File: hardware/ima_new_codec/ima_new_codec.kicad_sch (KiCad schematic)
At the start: 5 parts, among them J1 DM3AT-SF-PEJM5, U1 STM32F722RETx, Y3 Crystal_GND24

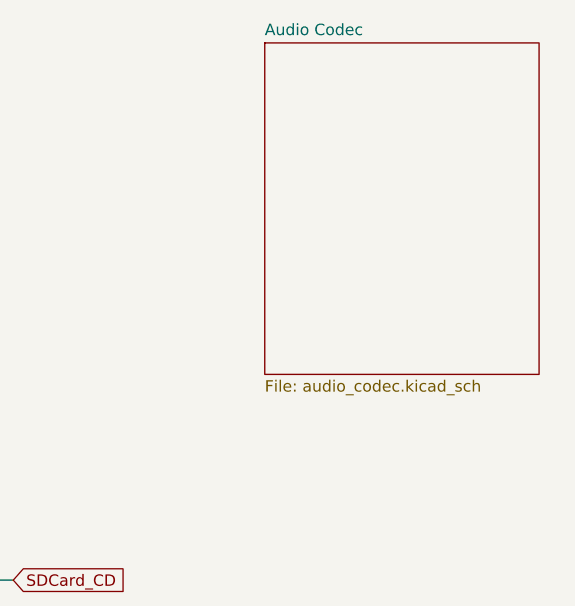
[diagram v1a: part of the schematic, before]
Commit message: changes to in/out stages
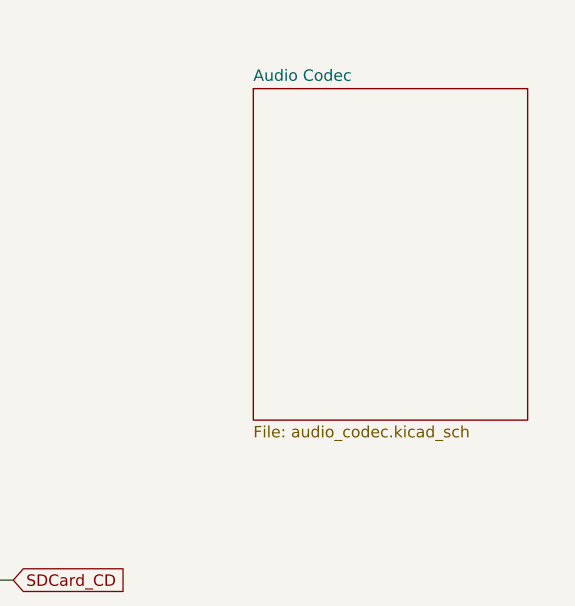
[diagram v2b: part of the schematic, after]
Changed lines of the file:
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@@
 	)
 	(sheet
-		(at 212.09 30.48)
+		(at 210.82 35.56)
 		(size 30.48 36.83)
 		(fields_autoplaced yes)
@@
 		)
 		(property "Sheetname" "Audio Codec"
-			(at 212.09 29.7684 0)
+			(at 210.82 34.8484 0)
 			(effects
 				(font
@@
 		)
 		(property "Sheetfile" "audio_codec.kicad_sch"
-			(at 212.09 67.8946 0)
+			(at 210.82 72.9746 0)
 			(effects
 				(font

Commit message: changes to hardware design
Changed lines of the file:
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@@
+	(wire
+		(pts
+			(xy 104.14 63.5) (xy 104.14 64.77)
+		)
+		(stroke
+			(width 0)
+			(type default)
+		)
+	)
 	(wire
 		(pts
@@
 	(wire
 		(pts
-			(xy 93.98 64.77) (xy 93.98 82.55)
-		)
-		(stroke
-			(width 0)
-			(type default)
-		)
-	)
-	(wire
-		(pts
-			(xy 104.14 64.77) (xy 93.98 64.77)
+			(xy 93.98 63.5) (xy 93.98 82.55)
+		)
+		(stroke
+			(width 0)
+			(type default)
+		)
+	)
+	(wire
+		(pts
+			(xy 104.14 63.5) (xy 93.98 63.5)
 		)
 		(stroke
@@
 		(dnp no)
 		(property "Reference" "Y3"
-			(at 104.902 63.5 0)
+			(at 105.664 63.5 0)
 			(effects
 				(font
@@
 		)
 		(property "Value" "Crystal_GND24"
-			(at 92.71 63.246 0)
-			(effects
-				(font
+			(at 92.71 61.976 0)
+			(effects
+				(font
